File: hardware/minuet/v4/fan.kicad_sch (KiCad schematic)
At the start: 8 parts, among them J8 B3P-VH-B, U5 MCF8316D

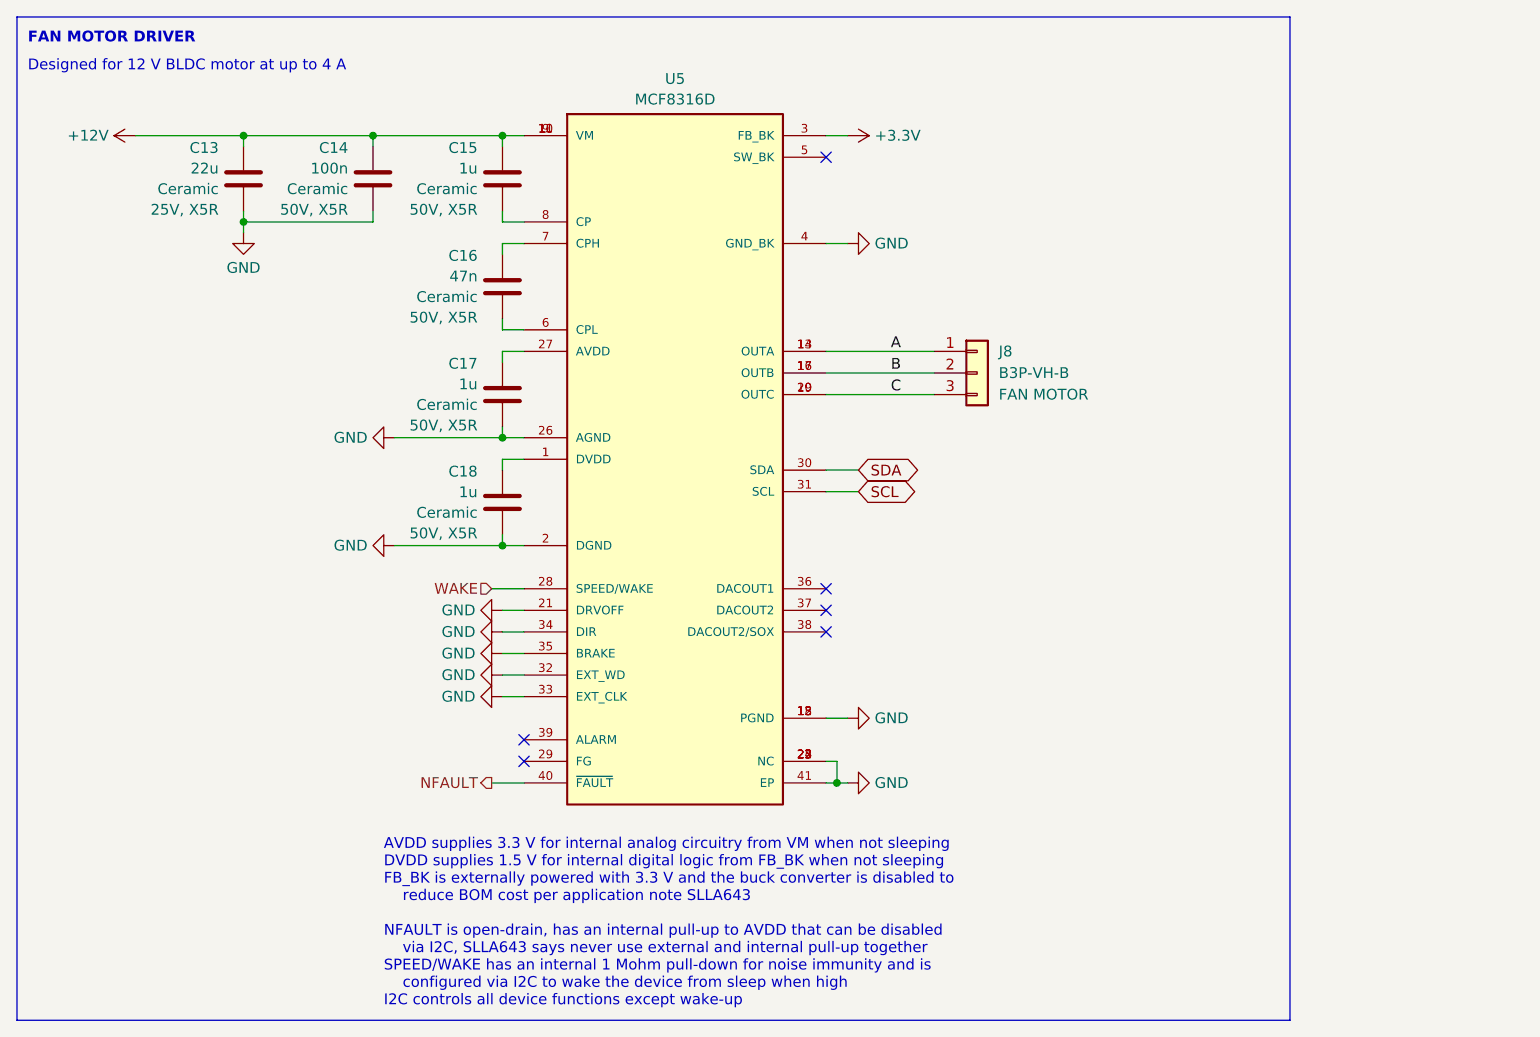
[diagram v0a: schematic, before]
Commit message: First draft of Minuet v4 fan controller board
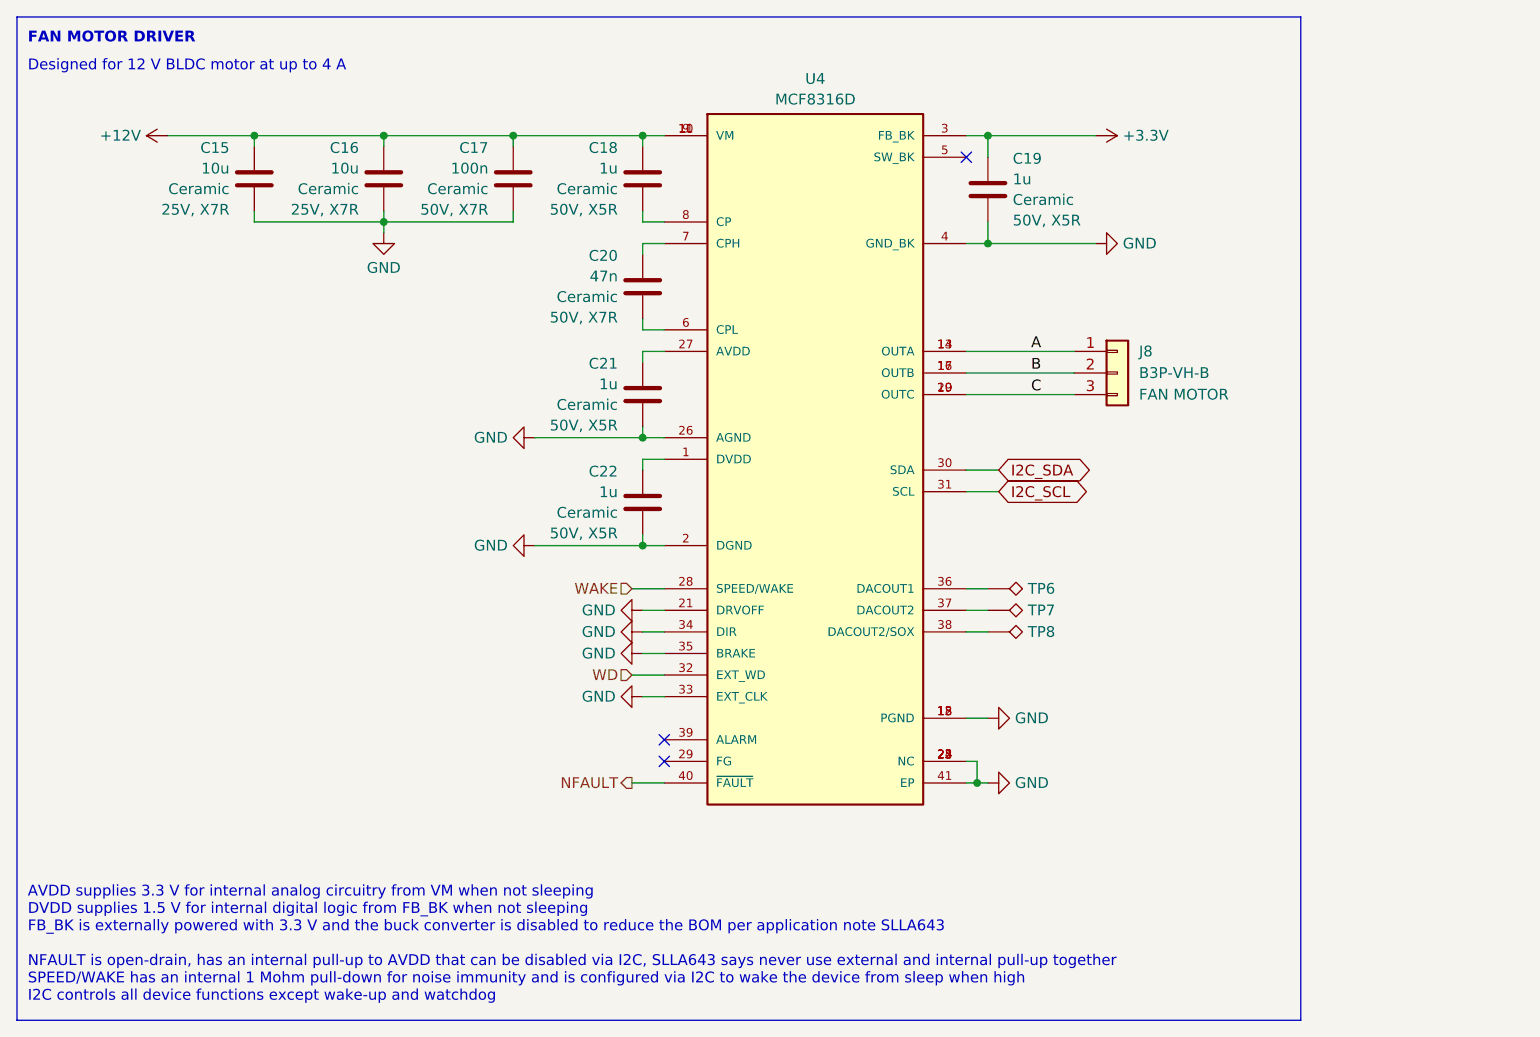
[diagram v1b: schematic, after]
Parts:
- removed C13: 22u, Capacitor_SMD:C_0805_2012Metric, symbol Device:C
- added C15, C16: 10u, Capacitor_SMD:C_1210_3225Metric, symbol Device:C
- added C19: 1u, Capacitor_SMD:C_0603_1608Metric, symbol Device:C
- added TP6, TP7, TP8: TestPoint_Alt, TestPoint:TestPoint_Pad_D1.0mm, symbol Connector:TestPoint_Alt
- C17: renamed from C14; Rating 50V, X5R -> 50V, X7R
- C20: renamed from C16; Rating 50V, X5R -> 50V, X7R
- renumbered C15 to C18, C17 to C21, C18 to C22, U5 to U4
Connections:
- net +12V: now also C15.1, C16.1
- net +3.3V: now also C19.1
- net GND: now also C15.2, C16.2, C19.2; no longer U4.32 (EXT_WD)
- net at U4.36 (DACOUT1): now also TP6.1
- net at U4.37 (DACOUT2): now also TP7.1
- net at U4.38 (DACOUT2/SOX): now also TP8.1
- net SCL renamed I2C_SCL
- net SDA renamed I2C_SDA
- new net WD: U4.32 (EXT_WD)
- no-connect marks 6 -> 3
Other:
- note added: "AVDD supplies 3.3 V for internal analog circuitry from VM when not sleeping DVDD supplies 1.5 V for internal digital logic from FB_BK when not sleeping FB_BK is externally powered with 3.3 V and the buck converter is disabled to reduce the BOM per application note SLLA643 NFAULT is open-drain, has an internal pull-up to AVDD that can be disabled via I2C, SLLA643 says never use external and intern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"
- note removed: "AVDD supplies 3.3 V for internal analog circuitry from VM when not sleeping DVDD supplies 1.5 V for internal digital logic from FB_BK when not sleeping FB_BK is externally powered with 3.3 V and the buck converter is disabled to reduce BOM cost per application note SLLA643 NFAULT is open-drain, has an internal pull-up to AVDD that can be disabled via I2C, SLLA643 says never use external and inter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"
- company: (none) -> Brown Studios LLC
- moved on the sheet: C17, C18, C20, C21, C22, J8, U4

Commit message: Second draft of Minuet v4 main board.
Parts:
- renumbered C15 to C16, C16 to C17, C17 to C18, C18 to C19, C19 to C20, C20 to C21, C21 to C22, C22 to C23, TP6 to TP5, TP7 to TP6, TP8 to TP7
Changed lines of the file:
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@@
 		(dnp no)
 		(fields_autoplaced yes)
-		(property "Reference" "#PWR041"
+		(property "Reference" "#PWR043"
 			(at 193.04 45.72 0)
 			(effects
@@
 			(project "minuet"
 				(path "/5bd7983a-3caa-4bb2-9dc5-1af533f31e50/26911c9c-0aba-4ac6-a40d-12dbad49caee"
-					(reference "#PWR041")
+					(reference "#PWR043")
 					(unit 1)
 				)
@@
 		(dnp no)
 		(fields_autoplaced yes)
-		(property "Reference" "#PWR046"
+		(property "Reference" "#PWR048"
 			(at 137.16 101.6 0)
 			(effects
@@
 			(project "minuet"
 				(path "/5bd7983a-3caa-4bb2-9dc5-1af533f31e50/26911c9c-0aba-4ac6-a40d-12dbad49caee"
-					(reference "#PWR046")
+					(reference "#PWR048")
 					(unit 1)
 				)
@@
 		(dnp no)
 		(fields_autoplaced yes)
-		(property "Reference" "C18"
+		(property "Reference" "C19"
 			(at 140.589 47.1635 0)
 			(effects
@@
 			(project "minuet"
 				(path "/5bd7983a-3caa-4bb2-9dc5-1af533f31e50/26911c9c-0aba-4ac6-a40d-12dbad49caee"
-					(reference "C18")
+					(reference "C19")
 					(unit 1)
 				)
@@
 		(on_board yes)
 		(dnp no)
-		(property "Reference" "C17"
+		(property "Reference" "C18"
 			(at 125.349 47.1635 0)
 			(effects
@@
 			(project "minuet"
 				(path "/5bd7983a-3caa-4bb2-9dc5-1af533f31e50/26911c9c-0aba-4ac6-a40d-12dbad49caee"
-					(reference "C17")
+					(reference "C18")
 					(unit 1)
 				)
@@
 		(on_board yes)
 		(dnp no)
-		(property "Reference" "C21"
+		(property "Reference" "C22"
 			(at 140.589 72.5635 0)
 			(effects
@@
 			(project "minuet"
 				(path "/5bd7983a-3caa-4bb2-9dc5-1af533f31e50/26911c9c-0aba-4ac6-a40d-12dbad49caee"
-					(reference "C21")
+					(reference "C22")
 					(unit 1)
 				)
@@
 		(on_board yes)
 		(dnp no)
-		(property "Reference" "C15"
+		(property "Reference" "C16"
 			(at 94.869 47.1635 0)
 			(effects
@@
 			(project "minuet"
 				(path "/5bd7983a-3caa-4bb2-9dc5-1af533f31e50/26911c9c-0aba-4ac6-a40d-12dbad49caee"
-					(reference "C15")
+					(reference "C16")
 					(unit 1)
 				)
@@
 		(dnp no)
 		(fields_autoplaced yes)
-		(property "Reference" "TP8"
+		(property "Reference" "TP7"
 			(at 188.849 104.14 90)
 			(effects
@@
 			(project "minuet"
 				(path "/5bd7983a-3caa-4bb2-9dc5-1af533f31e50/26911c9c-0aba-4ac6-a40d-12dbad49caee"
-					(reference "TP8")
+					(reference "TP7")
 					(unit 1)
 				)
@@
 		(dnp no)
 		(fields_autoplaced yes)
-		(property "Reference" "#PWR048"
+		(property "Reference" "#PWR050"
 			(at 137.16 106.68 0)
 			(effects
@@
 			(project "minuet"
 				(path "/5bd7983a-3caa-4bb2-9dc5-1af533f31e50/26911c9c-0aba-4ac6-a40d-12dbad49caee"
-					(reference "#PWR048")
+					(reference "#PWR050")
 					(unit 1)
 				)
@@
 		(dnp no)
 		(fields_autoplaced yes)
-		(property "Reference" "#PWR040"
+		(property "Reference" "#PWR042"
 			(at 91.44 45.72 0)
 			(effects
@@
 			(project "minuet"
 				(path "/5bd7983a-3caa-4bb2-9dc5-1af533f31e50/26911c9c-0aba-4ac6-a40d-12dbad49caee"
-					(reference "#PWR040")
+					(reference "#PWR042")
 					(unit 1)
 				)
@@
 		(dnp no)
 		(fields_autoplaced yes)
-		(property "Reference" "TP7"
+		(property "Reference" "TP6"
 			(at 188.849 101.6 90)
 			(effects
@@
 			(project "minuet"
 				(path "/5bd7983a-3caa-4bb2-9dc5-1af533f31e50/26911c9c-0aba-4ac6-a40d-12dbad49caee"
-					(reference "TP7")
+					(reference "TP6")
 					(unit 1)
 				)
@@
 		(on_board yes)
 		(dnp no)
-		(property "Reference" "C19"
+		(property "Reference" "C20"
 			(at 187.071 48.4335 0)
 			(effects
@@
 			(project "minuet"
 				(path "/5bd7983a-3caa-4bb2-9dc5-1af533f31e50/26911c9c-0aba-4ac6-a40d-12dbad49caee"
-					(reference "C19")
+					(reference "C20")
 					(unit 1)
 				)
@@
 		(dnp no)
 		(fields_autoplaced yes)
-		(property "Reference" "TP6"
+		(property "Reference" "TP5"
 			(at 188.849 99.06 90)
 			(effects
@@
 			(project ""
 				(path "/5bd7983a-3caa-4bb2-9dc5-1af533f31e50/26911c9c-0aba-4ac6-a40d-12dbad49caee"
-					(reference "TP6")
+					(reference "TP5")
 					(unit 1)
 				)
@@
 		(dnp no)
 		(fields_autoplaced yes)
-		(property "Reference" "#PWR049"
+		(property "Reference" "#PWR051"
 			(at 137.16 111.76 0)
 			(effects
@@
 			(project "minuet"
 				(path "/5bd7983a-3caa-4bb2-9dc5-1af533f31e50/26911c9c-0aba-4ac6-a40d-12dbad49caee"
-					(reference "#PWR049")
+					(reference "#PWR051")
 					(unit 1)
 				)
@@
 		(on_board yes)
 		(dnp no)
-		(property "Reference" "C22"
+		(property "Reference" "C23"
 			(at 140.589 85.2635 0)
 			(effects
@@
 			(project "minuet"
 				(path "/5bd7983a-3caa-4bb2-9dc5-1af533f31e50/26911c9c-0aba-4ac6-a40d-12dbad49caee"
-					(reference "C22")
+					(reference "C23")
 					(unit 1)
 				)
@@
 		(on_board yes)
 		(dnp no)
-		(property "Reference" "C16"
+		(property "Reference" "C17"
 			(at 110.109 47.1635 0)
 			(effects
@@
 			(project "minuet"
 				(path "/5bd7983a-3caa-4bb2-9dc5-1af533f31e50/26911c9c-0aba-4ac6-a40d-12dbad49caee"
-					(reference "C16")
+					(reference "C17")
 					(unit 1)
 				)
@@
 		(dnp no)
 		(fields_autoplaced yes)
-		(property "Reference" "#PWR045"
+		(property "Reference" "#PWR047"
 			(at 124.46 93.98 0)
 			(effects
@@
 			(project "minuet"
 				(path "/5bd7983a-3caa-4bb2-9dc5-1af533f31e50/26911c9c-0aba-4ac6-a40d-12dbad49caee"
-					(reference "#PWR045")
+					(reference "#PWR047")
 					(unit 1)
 				)
@@
 		(dnp no)
 		(fields_autoplaced yes)
-		(property "Reference" "#PWR042"
+		(property "Reference" "#PWR044"
 			(at 113.03 63.5 0)
 			(effects
@@
 			(project "minuet"
 				(path "/5bd7983a-3caa-4bb2-9dc5-1af533f31e50/26911c9c-0aba-4ac6-a40d-12dbad49caee"
-					(reference "#PWR042")
+					(reference "#PWR044")
 					(unit 1)
 				)
@@
 		(dnp no)
 		(fields_autoplaced yes)
-		(property "Reference" "#PWR050"
+		(property "Reference" "#PWR052"
 			(at 190.5 114.3 0)
 			(effects
@@
 			(project "minuet"
 				(path "/5bd7983a-3caa-4bb2-9dc5-1af533f31e50/26911c9c-0aba-4ac6-a40d-12dbad49caee"
-					(reference "#PWR050")
+					(reference "#PWR052")
 					(unit 1)
 				)
@@
 		(dnp no)
 		(fields_autoplaced yes)
-		(property "Reference" "C20"
+		(property "Reference" "C21"
 			(at 140.589 59.8635 0)
 			(effects
@@
 			(project "minuet"
 				(path "/5bd7983a-3caa-4bb2-9dc5-1af533f31e50/26911c9c-0aba-4ac6-a40d-12dbad49caee"
-					(reference "C20")
+					(reference "C21")
 					(unit 1)
 				)
@@
 		(dnp no)
 		(fields_autoplaced yes)
-		(property "Reference" "#PWR051"
+		(property "Reference" "#PWR053"
 			(at 190.5 121.92 0)
 			(effects
@@
 			(project "minuet"
 				(path "/5bd7983a-3caa-4bb2-9dc5-1af533f31e50/26911c9c-0aba-4ac6-a40d-12dbad49caee"
-					(reference "#PWR051")
+					(reference "#PWR053")
 					(unit 1)
 				)
@@
 		(dnp no)
 		(fields_autoplaced yes)
-		(property "Reference" "#PWR044"
+		(property "Reference" "#PWR046"
 			(at 124.46 81.28 0)
 			(effects
@@
 			(project "minuet"
 				(path "/5bd7983a-3caa-4bb2-9dc5-1af533f31e50/26911c9c-0aba-4ac6-a40d-12dbad49caee"
-					(reference "#PWR044")
+					(reference "#PWR046")
 					(unit 1)
 				)
@@
 		(dnp no)
 		(fields_autoplaced yes)
-		(property "Reference" "#PWR043"
+		(property "Reference" "#PWR045"
 			(at 203.2 58.42 0)
 			(effects
@@
 			(project "minuet"
 				(path "/5bd7983a-3caa-4bb2-9dc5-1af533f31e50/26911c9c-0aba-4ac6-a40d-12dbad49caee"
-					(reference "#PWR043")
+					(reference "#PWR045")
 					(unit 1)
 				)
@@
 		(dnp no)
 		(fields_autoplaced yes)
-		(property "Reference" "#PWR047"
+		(property "Reference" "#PWR049"
 			(at 137.16 104.14 0)
 			(effects
@@
 			(project "minuet"
 				(path "/5bd7983a-3caa-4bb2-9dc5-1af533f31e50/26911c9c-0aba-4ac6-a40d-12dbad49caee"
-					(reference "#PWR047")
-					(unit 1)
-				)
+					(reference "#PWR049")
+					(unit 1)
+				)

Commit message: Prepare main board for fabrication
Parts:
- added TP5: TestPoint_Alt, TestPoint:TestPoint_Pad_D1.0mm, symbol Connector:TestPoint_Alt
- renumbered TP5 to TP6, TP6 to TP7, TP7 to TP8
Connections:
- net GND: now also TP5.1
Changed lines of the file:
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@@
+	(wire
+		(pts
+			(xy 196.85 93.98) (xy 198.12 93.98)
+		)
+		(stroke
+			(width 0)
+			(type default)
+		)
+	)
 	(wire
 		(pts
@@
 		(dnp no)
 		(fields_autoplaced yes)
-		(property "Reference" "#PWR048"
+		(property "Reference" "#PWR049"
 			(at 137.16 101.6 0)
 			(effects
@@
 			(project "minuet"
 				(path "/5bd7983a-3caa-4bb2-9dc5-1af533f31e50/26911c9c-0aba-4ac6-a40d-12dbad49caee"
-					(reference "#PWR048")
+					(reference "#PWR049")
 					(unit 1)
 				)
@@
 	)
 	(symbol
+		(lib_id "power:GND")
+		(at 198.12 93.98 90)
+		(unit 1)
+		(exclude_from_sim no)
+		(in_bom yes)
+		(on_board yes)
+		(dnp no)
+		(fields_autoplaced yes)
+		(property "Reference" "#PWR048"
+			(at 204.47 93.98 0)
+			(effects
+				(font
+					(size 1.27 1.27)
+				)
+				(hide yes)
+			)
+		)
+		(property "Value" "GND"
+			(at 201.2949 93.98 90)
+			(effects
+				(font
+					(size 1.27 1.27)
+				)
+				(justify right)
+			)
+		)
+		(property "Footprint" ""
+			(at 198.12 93.98 0)
+			(effects
+				(font
+					(size 1.27 1.27)
+				)
+				(hide yes)
+			)
+		)
+		(property "Datasheet" ""
+			(at 198.12 93.98 0)
+			(effects
+				(font
+					(size 1.27 1.27)
+				)
+				(hide yes)
+			)
+		)
+		(property "Description" "Power symbol creates a global label with name \"GND\" , ground"
+			(at 198.12 93.98 0)
+			(effects
+				(font
+					(size 1.27 1.27)
+				)
+				(hide yes)
+			)
+		)
+		(pin "1"
+		)
+		(instances
+			(project "minuet"
+				(path "/5bd7983a-3caa-4bb2-9dc5-1af533f31e50/26911c9c-0aba-4ac6-a40d-12dbad49caee"
+					(reference "#PWR048")
+					(unit 1)
+				)
+			)
+		)
+	)
+	(symbol
 		(lib_id "Device:C")
 		(at 128.27 50.8 0)
@@
 		(dnp no)
 		(fields_autoplaced yes)
-		(property "Reference" "TP7"
+		(property "Reference" "TP8"
 			(at 188.849 104.14 90)
 			(effects
@@
 			(project "minuet"
 				(path "/5bd7983a-3caa-4bb2-9dc5-1af533f31e50/26911c9c-0aba-4ac6-a40d-12dbad49caee"
-					(reference "TP7")
+					(reference "TP8")
 					(unit 1)
 				)
@@
 		(dnp no)
 		(fields_autoplaced yes)
-		(property "Reference" "#PWR050"
+		(property "Reference" "#PWR051"
 			(at 137.16 106.68 0)
 			(effects
@@
 			(project "minuet"
 				(path "/5bd7983a-3caa-4bb2-9dc5-1af533f31e50/26911c9c-0aba-4ac6-a40d-12dbad49caee"
-					(reference "#PWR050")
+					(reference "#PWR051")
 					(unit 1)
 				)
@@
 		(dnp no)
 		(fields_autoplaced yes)
-		(property "Reference" "TP6"
+		(property "Reference" "TP7"
 			(at 188.849 101.6 90)
 			(effects
@@
 			(project "minuet"
 				(path "/5bd7983a-3caa-4bb2-9dc5-1af533f31e50/26911c9c-0aba-4ac6-a40d-12dbad49caee"
-					(reference "TP6")
+					(reference "TP7")
 					(unit 1)
 				)
@@
 		(dnp no)
 		(fields_autoplaced yes)
-		(property "Reference" "TP5"
+		(property "Reference" "TP6"
 			(at 188.849 99.06 90)
 			(effects
@@
 			(project ""
 				(path "/5bd7983a-3caa-4bb2-9dc5-1af533f31e50/26911c9c-0aba-4ac6-a40d-12dbad49caee"
-					(reference "TP5")
+					(reference "TP6")
 					(unit 1)
 				)
@@
 		(dnp no)
 		(fields_autoplaced yes)
-		(property "Reference" "#PWR051"
+		(property "Reference" "#PWR052"
 			(at 137.16 111.76 0)
 			(effects
@@
 			(project "minuet"
 				(path "/5bd7983a-3caa-4bb2-9dc5-1af533f31e50/26911c9c-0aba-4ac6-a40d-12dbad49caee"
-					(reference "#PWR051")
+					(reference "#PWR052")
 					(unit 1)
 				)
@@
 		(dnp no)
 		(fields_autoplaced yes)
-		(property "Reference" "#PWR052"
+		(property "Reference" "#PWR053"
 			(at 190.5 114.3 0)
 			(effects
@@
 			(project "minuet"
 				(path "/5bd7983a-3caa-4bb2-9dc5-1af533f31e50/26911c9c-0aba-4ac6-a40d-12dbad49caee"
-					(reference "#PWR052")
+					(reference "#PWR053")
 					(unit 1)
 				)
@@
 		(dnp no)
 		(fields_autoplaced yes)
-		(property "Reference" "#PWR053"
+		(property "Reference" "#PWR054"
 			(at 190.5 121.92 0)
 			(effects
@@
 			(project "minuet"
 				(path "/5bd7983a-3caa-4bb2-9dc5-1af533f31e50/26911c9c-0aba-4ac6-a40d-12dbad49caee"
-					(reference "#PWR053")
+					(reference "#PWR054")
+					(unit 1)
+				)
+			)
+		)
+	)
+	(symbol
+		(lib_id "Connector:TestPoint_Alt")
+		(at 196.85 93.98 90)
+		(unit 1)
+		(exclude_from_sim no)
+		(in_bom no)
+		(on_board yes)
+		(dnp no)
+		(fields_autoplaced yes)
+		(property "Reference" "TP5"
+			(at 192.151 93.98 90)
+			(effects
+				(font
+					(size 1.27 1.27)
+				)
+				(justify left)
+			)
+		)
+		(property "Value" "TestPoint_Alt"
+			(at 192.151 92.7679 90)
+			(effects
+				(font
+					(size 1.27 1.27)
+				)
+				(justify left)
+				(hide yes)
+			)
+		)
+		(property "Footprint" "TestPoint:TestPoint_Pad_D1.0mm"
+			(at 196.85 88.9 0)
+			(effects
+				(font
+					(size 1.27 1.27)
+				)
+				(hide yes)
+			)
+		)
+		(property "Datasheet" "~"
+			(at 196.85 88.9 0)
+			(effects
+				(font
+					(size 1.27 1.27)
+				)
+				(hide yes)
+			)
+		)
+		(property "Description" "test point (alternative shape)"
+			(at 196.85 93.98 0)
+			(effects
+				(font
+					(size 1.27 1.27)
+				)
+				(hide yes)
+			)
+		)
+		(pin "1"
+		)
+		(instances
+			(project "minuet"
+				(path "/5bd7983a-3caa-4bb2-9dc5-1af533f31e50/26911c9c-0aba-4ac6-a40d-12dbad49caee"
+					(reference "TP5")
 					(unit 1)
 				)
@@
 		(dnp no)
 		(fields_autoplaced yes)
-		(property "Reference" "#PWR049"
+		(property "Reference" "#PWR050"
 			(at 137.16 104.14 0)
 			(effects
@@
 			(project "minuet"
 				(path "/5bd7983a-3caa-4bb2-9dc5-1af533f31e50/26911c9c-0aba-4ac6-a40d-12dbad49caee"
-					(reference "#PWR049")
-					(unit 1)
-				)
+					(reference "#PWR050")
+					(unit 1)
+				)
